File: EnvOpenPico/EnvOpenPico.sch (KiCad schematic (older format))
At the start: 51 parts, among them J1 SKRKAEE020, J2 SKRKAEE020, J3 2.54mm header 01x20, J4 2.54mm header 01x20, J5 Conn_01x03_Male, U1 TLV75533PDBVR, U3 RP2040, Y1 Crystal

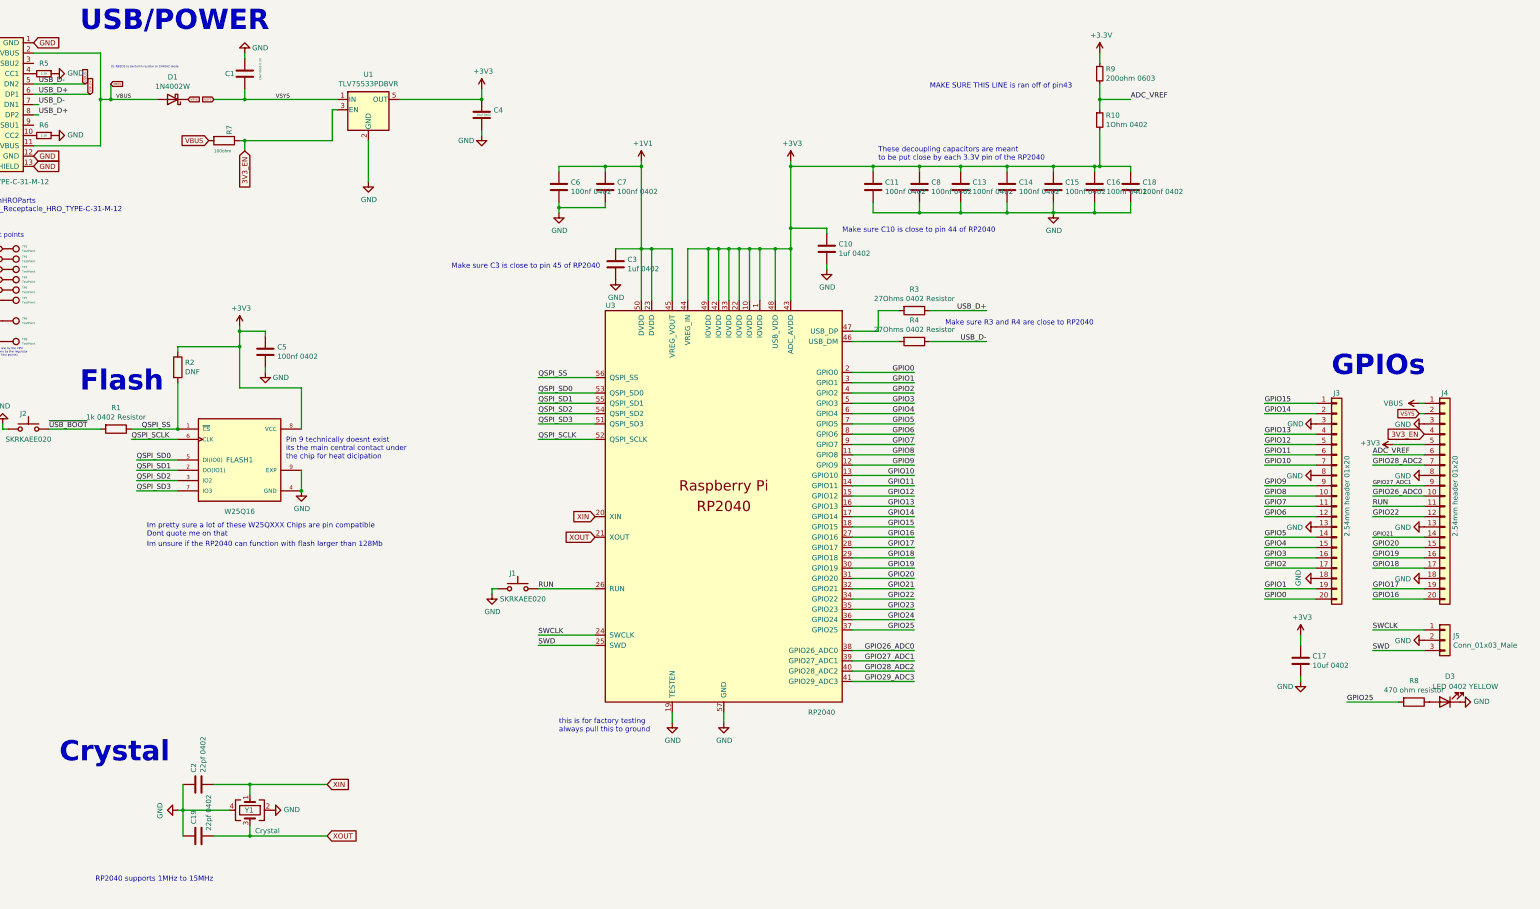
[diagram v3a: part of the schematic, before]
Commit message: changed some labels to make part selection easier
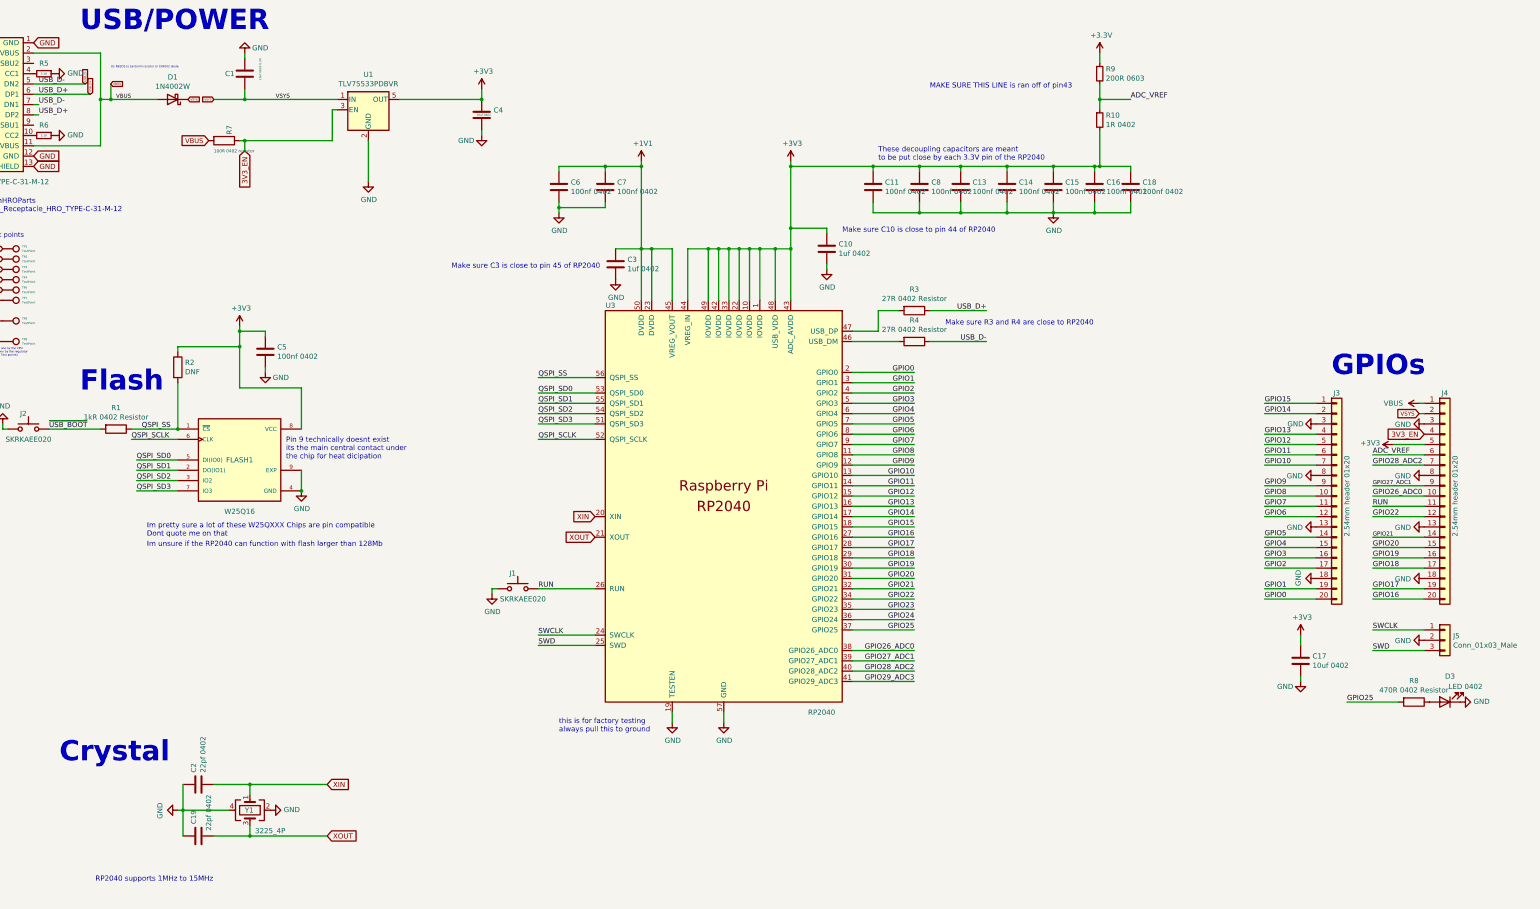
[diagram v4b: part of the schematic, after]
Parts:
- D3: value LED 0402 YELLOW -> LED 0402
- R1: value 1k 0402 Resistor -> 1kR 0402 Resistor
- R10: value 1Ohm 0402 -> 1R 0402
- R3, R4: value 27Ohms 0402 Resistor -> 27R 0402 Resistor
- R7: value 100ohm -> 100R 0402 resistor
- R8: value 470 ohm resistor -> 470R 0402 Resistor
- R9: value 200ohm 0603 -> 200R 0603
- Y1: value Crystal -> 3225_4P
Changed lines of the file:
@@
 P 9650 4100
 F 0 "R4" V 9443 4100 50  0000 C CNN
-F 1 " 27Ohms 0402 Resistor" V 9534 4100 50  0000 C CNN
+F 1 "27R 0402 Resistor" V 9534 4100 50  0000 C CNN
 F 2 "Capacitor_SMD:C_0402_1005Metric" V 9580 4100 50  0001 C CNN
 F 3 "" H 9650 4100 50  0001 C CNN
@@
 P 1900 4950
 F 0 "R1" V 1693 4950 50  0000 C CNN
-F 1 "1k 0402 Resistor" V 1784 4950 50  0000 C CNN
+F 1 "1kR 0402 Resistor" V 1784 4950 50  0000 C CNN
 F 2 "Capacitor_SMD:C_0402_1005Metric" V 1830 4950 50  0001 C CNN
 F 3 "" H 1900 4950 50  0001 C CNN
@@
 P 9650 3800
 F 0 "R3" V 9443 3800 50  0000 C CNN
-F 1 " 27Ohms  0402 Resistor" V 9534 3800 50  0000 C CNN
+F 1 "27R 0402 Resistor" V 9534 3800 50  0000 C CNN
 F 2 "Capacitor_SMD:C_0402_1005Metric" V 9580 3800 50  0001 C CNN
 F 3 "" H 9650 3800 50  0001 C CNN
@@
 P 14500 7600
 F 0 "R8" V 14293 7600 50  0000 C CNN
-F 1 "470 ohm resistor" V 14384 7600 50  0000 C CNN
+F 1 "470R 0402 Resistor" V 14384 7600 50  0000 C CNN
 F 2 "Resistor_SMD:R_0402_1005Metric" V 14430 7600 50  0001 C CNN
 F 3 "" H 14500 7600 50  0001 C CNN
@@
 P 14800 7600
 F 0 "D3" H 14750 7350 50  0000 C CNN
-F 1 "LED 0402 YELLOW" H 14600 7450 50  0000 C CNN
+F 1 "LED 0402" H 14600 7450 50  0000 C CNN
 F 2 "LED_SMD:LED_0402_1005Metric" H 14800 7600 50  0001 C CNN
 F 3 "" H 14800 7600 50  0001 C CNN
@@
 P 2950 2150
 F 0 "R7" H 2800 2200 50  0000 L CNN
-F 1 "100ohm" V 3050 2050 30  0000 L CNN
+F 1 "100R 0402 resistor" V 3050 2050 30  0000 L CNN
 F 2 "Resistor_SMD:R_0402_1005Metric" V 2880 2150 50  0001 C CNN
 F 3 "" H 2950 2150 50  0001 C CNN
@@
 P 11450 1950
 F 0 "R10" H 11509 1996 50  0000 L CNN
-F 1 "1Ohm 0402" H 11509 1905 50  0000 L CNN
+F 1 "1R 0402" H 11509 1905 50  0000 L CNN
 F 2 "Resistor_SMD:R_0402_1005Metric" H 11450 1950 50  0001 C CNN
 F 3 "~" H 11450 1950 50  0001 C CNN
@@
 P 11450 1500
 F 0 "R9" H 11509 1546 50  0000 L CNN
-F 1 "200ohm 0603" H 11509 1455 50  0000 L CNN
+F 1 "200R 0603" H 11509 1455 50  0000 L CNN
 F 2 "Resistor_SMD:R_0603_1608Metric" H 11450 1500 50  0001 C CNN
 F 3 "~" H 11450 1500 50  0001 C CNN
@@
 P 3200 8650
 F 0 "Y1" V 3200 8600 50  0000 L CNN
-F 1 "Crystal" V 3400 8700 50  0000 L CNN
+F 1 "3225_4P" V 3400 8700 50  0000 L CNN
 F 2 "Crystal:Crystal_SMD_3225-4Pin_3.2x2.5mm" H 3200 8650 50  0001 C CNN
 F 3 "~" H 3200 8650 50  0001 C CNN

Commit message: added a optinal bypass resistor cBP1 incase an alternative SOT-23-5 regulator is installed. + moved more pinout silkscreen to the front.
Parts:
- added cBP1: 10uf 0402, Capacitor_SMD:C_0402_1005Metric, symbol Device:C
- U1: symbol Regulator_Linear:TLV75533PDBV -> Regulator_Linear:AP131-15
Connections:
- net GND: now also cBP1.2
- net at U1.4 (BP): now also cBP1.1
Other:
- note added: "DO.NOT.FIT"
- note added: "MAKE SURE THIS LINE is ran off of pin43\nor close to pin43"
- note added: "Only fit cBP1 if you have selected an \nalternate voltage regulator\n\nTLV75533PDBVR does not."
- note removed: "MAKE SURE THIS LINE is ran off of pin43"
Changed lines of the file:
@@
 	1    0    0    -1
 $EndComp
-Text Notes 1700 9350 0    50   ~ 0
+Text Notes 2600 9100 0    50   ~ 0
 RP2040 supports 1MHz to 15MHz
 Text Notes 2200 6000 0    50   ~ 0
@@
 ADC_VREF
 Text Notes 9800 1650 0    50   ~ 0
-MAKE SURE THIS LINE is ran off of pin43
+MAKE SURE THIS LINE is ran off of pin43\nor close to pin43
 Text Label 14100 5200 0    50   ~ 0
 ADC_VREF
@@
 	5550 6500 5550 6550
 $Comp
-L Regulator_Linear:TLV75533PDBV U1
+L Regulator_Linear:AP131-15 U1
 U 1 1 6128F962
 P 4350 1850
@@
 Wire Wire Line
 	4350 2150 4350 2550
+$Comp
+L Device:C cBP1
+U 1 1 6127D24E
+P 4700 2050
+F 0 "cBP1" H 4815 2096 50  0000 L CNN
+F 1 "10uf 0402" H 4650 2050 20  0000 L CNN
+F 2 "Capacitor_SMD:C_0402_1005Metric" H 4738 1900 50  0001 C CNN
+F 3 "" H 4700 2050 50  0001 C CNN
+	1    4700 2050
+	1    0    0    -1
+$EndComp
+$Comp
+L power:GND #PWR0110
+U 1 1 6127D922
+P 4700 2250
+F 0 "#PWR0110" H 4700 2000 50  0001 C CNN
+F 1 "GND" H 4550 2200 50  0000 C CNN
+F 2 "" H 4700 2250 50  0001 C CNN
+F 3 "" H 4700 2250 50  0001 C CNN
+	1    4700 2250
+	1    0    0    -1
+$EndComp
+Wire Wire Line
+	4700 2250 4700 2200
+Wire Wire Line
+	4700 1900 4700 1850
+Wire Wire Line
+	4700 1850 4650 1850
+Text Notes 4450 2700 0    50   Italic 0
+Only fit cBP1 if you have selected an \nalternate voltage regulator\n\nTLV75533PDBVR does not.
+Text Notes 2500 4550 0    50   Italic 10
+DO.NOT.FIT
 $EndSCHEMATC

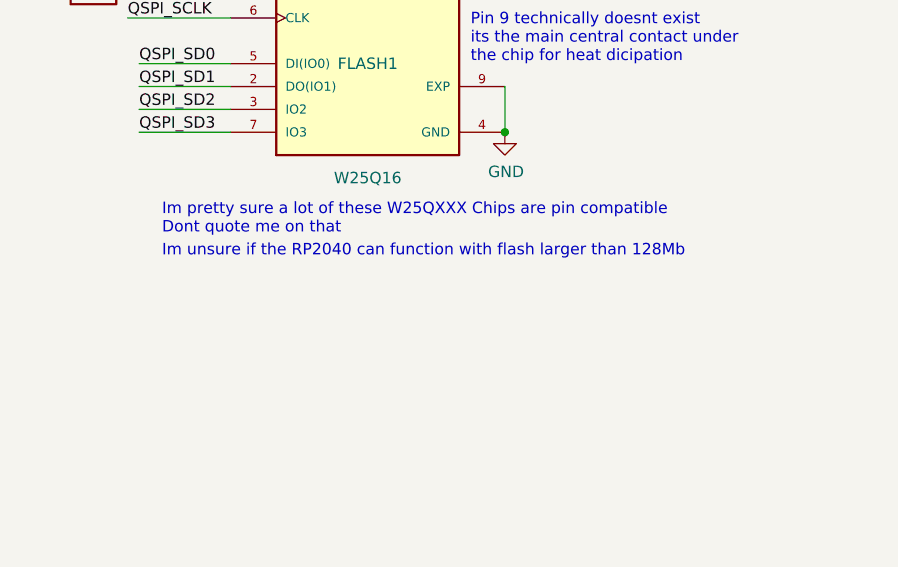
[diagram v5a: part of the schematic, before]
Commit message: Added a small note on a stocked Flash IC that JLC has loads of (as of right now.)
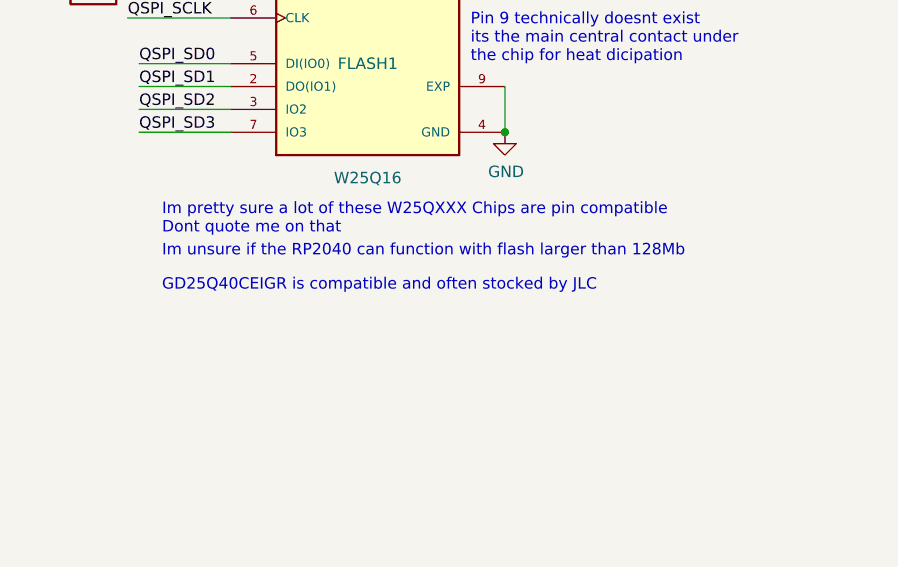
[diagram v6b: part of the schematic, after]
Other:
- note added: "GD25Q40CEIGR is compatible and often stocked by JLC"
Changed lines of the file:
@@
 Text Notes 2500 4550 0    50   Italic 10
 DO.NOT.FIT
+Text Notes 2200 6250 0    50   ~ 0
+GD25Q40CEIGR is compatible and often stocked by JLC
 $EndSCHEMATC

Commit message: Swapped type-c port footprint for hand solder version.
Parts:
- R1: value 1kR 0402 Resistor -> 1kΩ 0402 Resistor
- R10: value 1R 0402 -> 1Ω 0402
- R3, R4: value 27R 0402 Resistor -> 27Ω 0402 Resistor
- R5, R6: value 5.1K -> 5.1KΩ
- R7: value 100R 0402 resistor -> 100Ω 0402 resistor
- R8: value 470R 0402 Resistor -> 470Ω 0402 Resistor
- R9: value 200R 0603 -> 200Ω 0603
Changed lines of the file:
@@
 P 9650 4100
 F 0 "R4" V 9443 4100 50  0000 C CNN
-F 1 "27R 0402 Resistor" V 9534 4100 50  0000 C CNN
+F 1 "27Ω 0402 Resistor" V 9534 4100 50  0000 C CNN
 F 2 "Capacitor_SMD:C_0402_1005Metric" V 9580 4100 50  0001 C CNN
 F 3 "" H 9650 4100 50  0001 C CNN
@@
 P 1900 4950
 F 0 "R1" V 1693 4950 50  0000 C CNN
-F 1 "1kR 0402 Resistor" V 1784 4950 50  0000 C CNN
+F 1 "1kΩ 0402 Resistor" V 1784 4950 50  0000 C CNN
 F 2 "Capacitor_SMD:C_0402_1005Metric" V 1830 4950 50  0001 C CNN
 F 3 "" H 1900 4950 50  0001 C CNN
@@
 P 9650 3800
 F 0 "R3" V 9443 3800 50  0000 C CNN
-F 1 "27R 0402 Resistor" V 9534 3800 50  0000 C CNN
+F 1 "27Ω 0402 Resistor" V 9534 3800 50  0000 C CNN
 F 2 "Capacitor_SMD:C_0402_1005Metric" V 9580 3800 50  0001 C CNN
 F 3 "" H 9650 3800 50  0001 C CNN
@@
 P 14500 7600
 F 0 "R8" V 14293 7600 50  0000 C CNN
-F 1 "470R 0402 Resistor" V 14384 7600 50  0000 C CNN
+F 1 "470Ω 0402 Resistor" V 14384 7600 50  0000 C CNN
 F 2 "Resistor_SMD:R_0402_1005Metric" V 14430 7600 50  0001 C CNN
 F 3 "" H 14500 7600 50  0001 C CNN
@@
 P 1200 2100
 F 0 "R6" V 1100 2100 50  0000 C CNN
-F 1 "5.1K" V 1200 2100 20  0000 C CNN
+F 1 "5.1KΩ" V 1200 2100 20  0000 C CNN
 F 2 "Resistor_SMD:R_0402_1005Metric" H 1200 2100 50  0001 C CNN
 F 3 "" H 1200 2100 50  0001 C CNN
@@
 P 1200 1500
 F 0 "R5" V 1100 1500 50  0000 C CNN
-F 1 "5.1K" V 1200 1500 20  0000 C CNN
+F 1 "5.1KΩ" V 1200 1500 20  0000 C CNN
 F 2 "Resistor_SMD:R_0402_1005Metric" H 1200 1500 50  0001 C CNN
 F 3 "" H 1200 1500 50  0001 C CNN
@@
 P 2950 2150
 F 0 "R7" H 2800 2200 50  0000 L CNN
-F 1 "100R 0402 resistor" V 3050 2050 30  0000 L CNN
+F 1 "100Ω 0402 resistor" V 3050 2050 30  0000 L CNN
 F 2 "Resistor_SMD:R_0402_1005Metric" V 2880 2150 50  0001 C CNN
 F 3 "" H 2950 2150 50  0001 C CNN
@@
 P 11450 1950
 F 0 "R10" H 11509 1996 50  0000 L CNN
-F 1 "1R 0402" H 11509 1905 50  0000 L CNN
+F 1 "1Ω 0402" H 11509 1905 50  0000 L CNN
 F 2 "Resistor_SMD:R_0402_1005Metric" H 11450 1950 50  0001 C CNN
 F 3 "~" H 11450 1950 50  0001 C CNN
@@
 P 11450 1500
 F 0 "R9" H 11509 1546 50  0000 L CNN
-F 1 "200R 0603" H 11509 1455 50  0000 L CNN
+F 1 "200Ω 0603" H 11509 1455 50  0000 L CNN
 F 2 "Resistor_SMD:R_0603_1608Metric" H 11450 1500 50  0001 C CNN
 F 3 "~" H 11450 1500 50  0001 C CNN

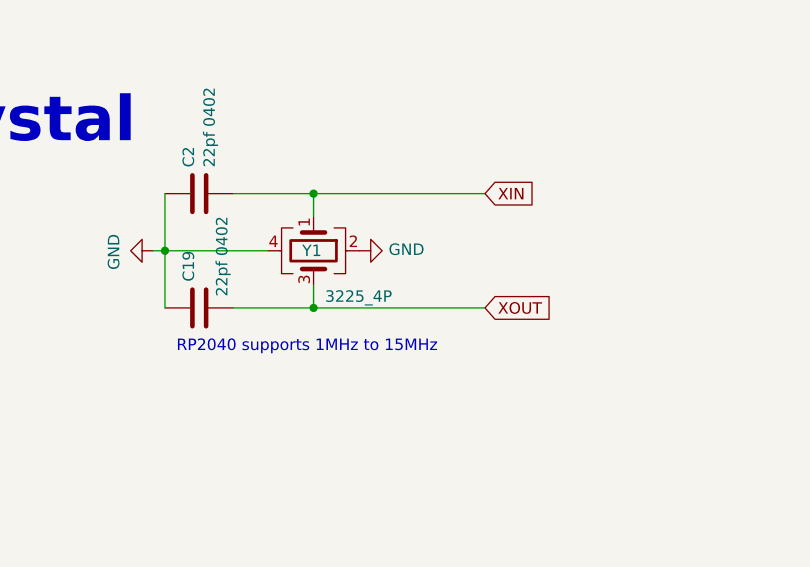
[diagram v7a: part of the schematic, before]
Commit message: added a resistor that I missed and once again generated updated gerbers lol.
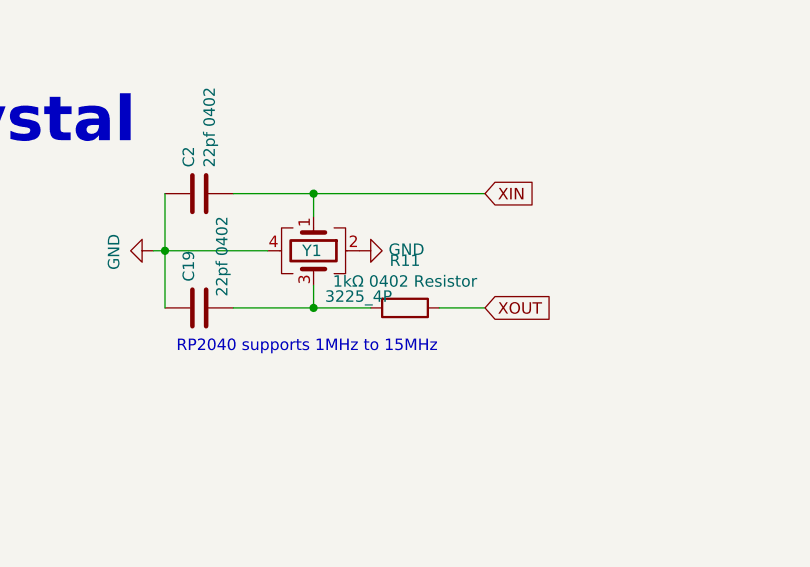
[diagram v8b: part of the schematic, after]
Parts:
- added R11: 1kΩ 0402 Resistor, Capacitor_SMD:C_0402_1005Metric, symbol Device:R
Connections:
- net XOUT: now also R11.1; no longer C19.2, Y1.3
- new net: C19.2, R11.2, Y1.3
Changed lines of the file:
@@
 Wire Wire Line
 	3200 8900 2850 8900
-Connection ~ 3200 8900
 Wire Wire Line
 	2850 8400 3200 8400
@@
 Wire Wire Line
 	3200 8400 3950 8400
-Wire Wire Line
-	3200 8900 3950 8900
 Text GLabel 6550 5800 0    50   Input ~ 0
 XIN
@@
 Text Notes 2200 6250 0    50   ~ 0
 GD25Q40CEIGR is compatible and often stocked by JLC
+$Comp
+L Device:R R11
+U 1 1 6150E6AB
+P 3600 8900
+F 0 "R11" V 3393 8900 50  0000 C CNN
+F 1 "1kΩ 0402 Resistor" V 3484 8900 50  0000 C CNN
+F 2 "Capacitor_SMD:C_0402_1005Metric" V 3530 8900 50  0001 C CNN
+F 3 "" H 3600 8900 50  0001 C CNN
+	1    3600 8900
+	0    1    1    0
+$EndComp
+Wire Wire Line
+	3750 8900 3950 8900
+Wire Wire Line
+	3450 8900 3200 8900
+Connection ~ 3200 8900
 $EndSCHEMATC
